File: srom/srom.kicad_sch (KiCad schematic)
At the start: 18 parts, among them J1 Conn_01x03_Female, Q1 PMBT2222A, U1 4075, U4 74LS245, U5 Pico-1 ROM

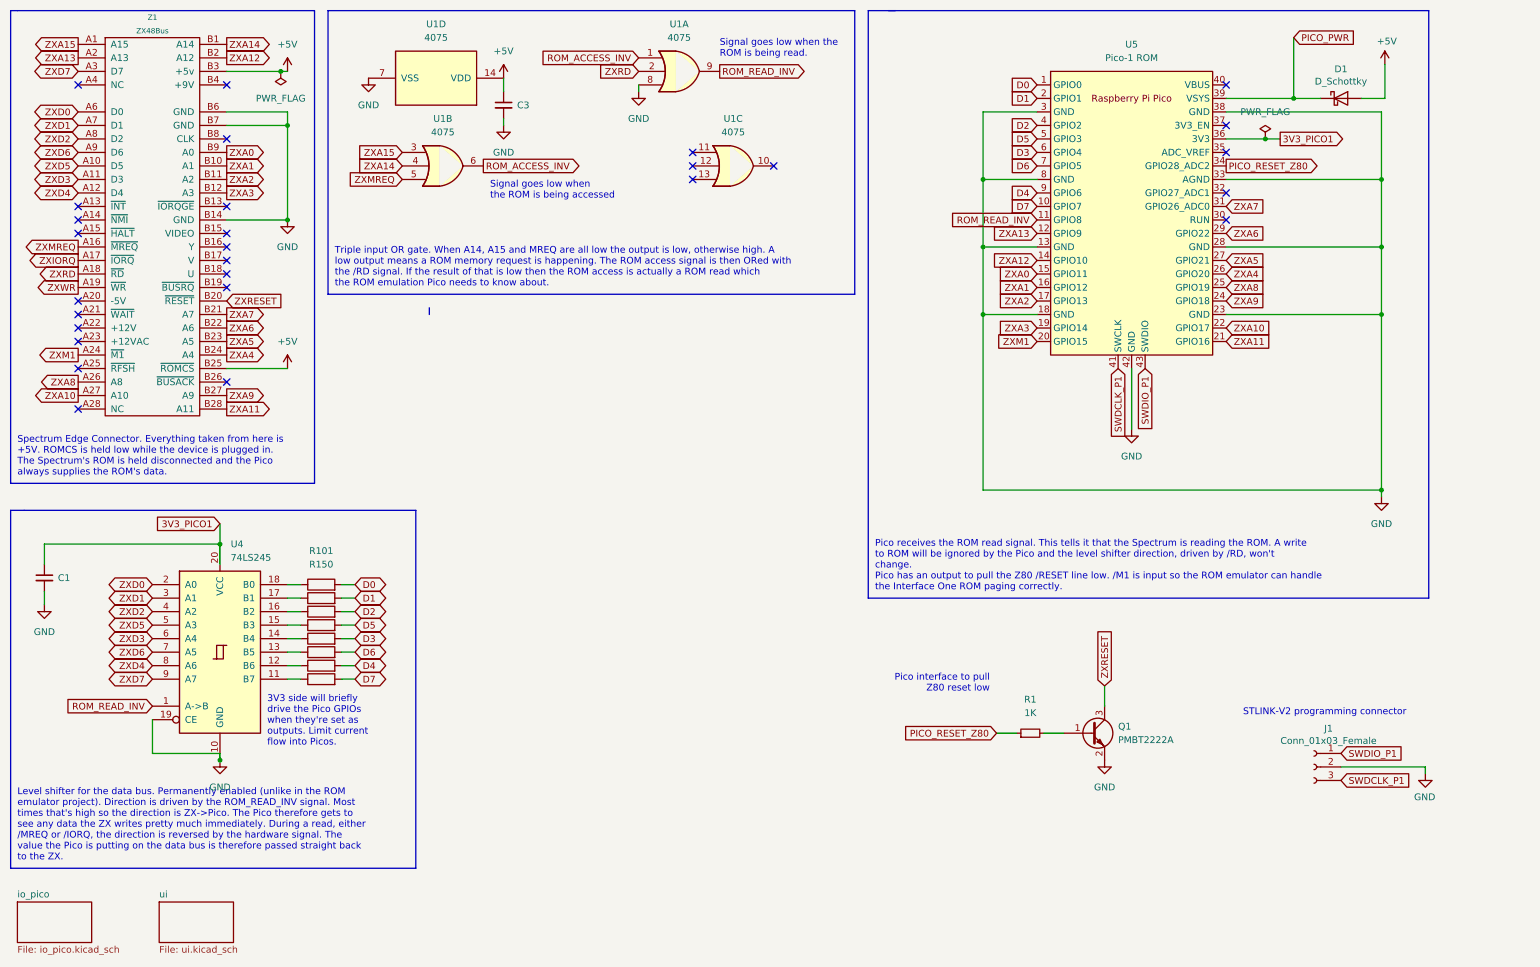
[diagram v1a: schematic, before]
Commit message: update schematic to match my modified prototype hardware
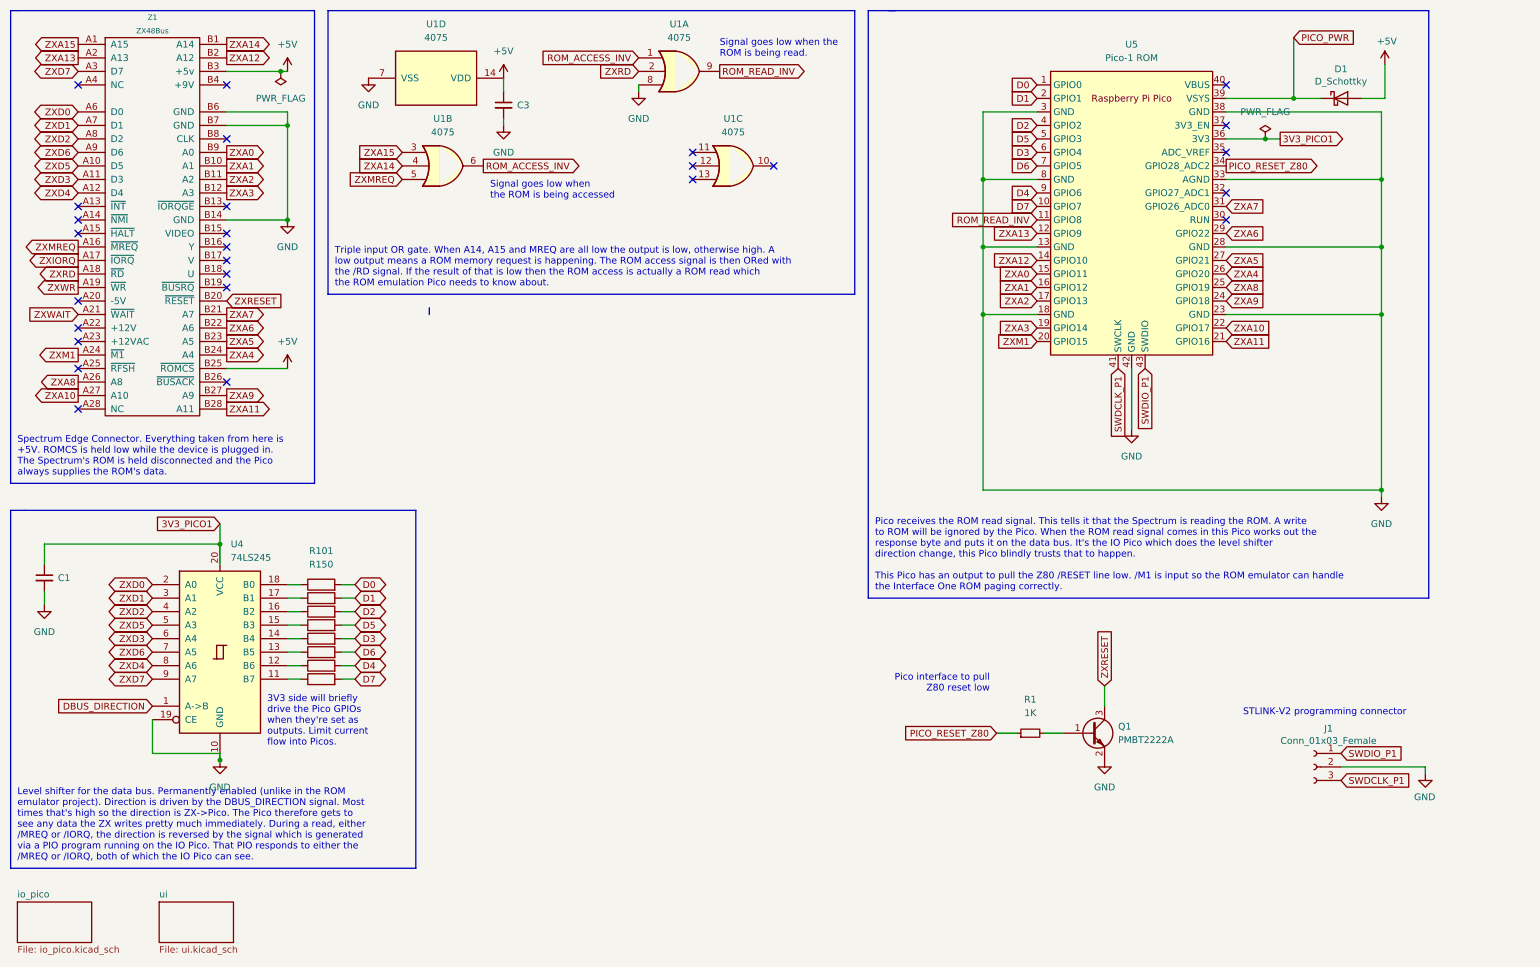
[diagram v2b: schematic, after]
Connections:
- net ROM_READ_INV: no longer U4.1 (A->B)
- net ZXWAIT: now reaches Z1.A21 (~{WAIT})
- new net DBUS_DIRECTION: U4.1 (A->B)
- no-connect marks 28 -> 27
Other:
- note added: "Level shifter for the data bus. Permanently enabled (unlike in the ROM emulator project). Direction is driven by the DBUS_DIRECTION signal. Most times that's high so the direction is ZX->Pico. The Pico therefore gets to see any data the ZX writes pretty much immediately. During a read, either /MREQ or /IORQ, the direction is reversed by the signal which is generated via a PIO program running on t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"
- note added: "Pico receives the ROM read signal. This tells it that the Spectrum is reading the ROM. A write to ROM will be ignored by the Pico. When the ROM read signal comes in this Pico works out the response byte and puts it on the data bus. It's the IO Pico which does the level shifter direction change, this Pico blindly trusts that to happen. This Pico has an output to pull the Z80 /RESET line low. /M1 i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"
- note removed: "Level shifter for the data bus. Permanently enabled (unlike in the ROM emulator project). Direction is driven by the ROM_READ_INV signal. Most times that's high so the direction is ZX->Pico. The Pico therefore gets to see any data the ZX writes pretty much immediately. During a read, either /MREQ or /IORQ, the direction is reversed by the hardware signal. The value the Pico is putting on the data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"
- note removed: "Pico receives the ROM read signal. This tells it that the Spectrum is reading the ROM. A write to ROM will be ignored by the Pico and the level shifter direction, driven by /RD, won't change. Pico has an output to pull the Z80 /RESET line low. /M1 is input so the ROM emulator can handle the Interface One ROM paging correctly."
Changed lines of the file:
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@@
   (no_connect (at 242.57 36.83))
   (no_connect (at 142.24 46.99))
-  (no_connect (at 26.67 72.39))
   (no_connect (at 26.67 69.85))
   (no_connect (at 54.61 52.07))
@@
     (stroke (width 0) (type default) (color 0 0 0 0))
   )
-  (text "Pico receives the ROM read signal. This tells it that the Spectrum is reading the ROM. A write\nto ROM will be ignored by the Pico and the level shifter direction, driven by /RD, won't\nchange.\nPico has an output to pull the Z80 /RESET line low. /M1 is input so the ROM emulator can handle\nthe Interface One ROM paging correctly."
+  (text "Pico receives the ROM read signal. This tells it that the Spectrum is reading the ROM. A write\nto ROM will be ignored by the Pico. When the ROM read signal comes in this Pico works out the\nresponse byte and puts it on the data bus. It's the IO Pico which does the level shifter\ndirection change, this Pico blindly trusts that to happen.\n\nThis Pico has an output to pull the Z80 /RESET line low. /M1 is input so the ROM emulator can handle\nthe Interface One ROM paging correctly."
     (at 176.53 124.46 0)
     (effects (font (size 1.27 1.27)) (justify left bottom))
   )
-  (text "Level shifter for the data bus. Permanently enabled (unlike in the ROM\nemulator project). Direction is driven by the ROM_READ_INV signal. Most\ntimes that's high so the direction is ZX->Pico. The Pico therefore gets to\nsee any data the ZX writes pretty much immediately. During a read, either\n/MREQ or /IORQ, the direction is reversed by the hardware signal. The\nvalue the Pico is putting on the data bus is therefore passed straight back\nto the ZX."
+  (text "Level shifter for the data bus. Permanently enabled (unlike in the ROM\nemulator project). Direction is driven by the DBUS_DIRECTION signal. Most\ntimes that's high so the direction is ZX->Pico. The Pico therefore gets to\nsee any data the ZX writes pretty much immediately. During a read, either\n/MREQ or /IORQ, the direction is reversed by the signal which is generated\nvia a PIO program running on the IO Pico. That PIO responds to either the\n/MREQ or /IORQ, both of which the IO Pico can see."
     (at 15.24 175.26 0)
     (effects (font (size 1.27 1.27)) (justify left bottom))
@@
     )
   )
-  (global_label "ROM_READ_INV" (shape input) (at 40.64 146.05 180) (fields_autoplaced)
-    (effects (font (size 1.27 1.27)) (justify right))
-    (property "Intersheet References" "${INTERSHEET_REFS}" (id 0) (at 24.4383 145.9706 0)
+  (global_label "DBUS_DIRECTION" (shape input) (at 40.64 146.05 180) (fields_autoplaced)
+    (effects (font (size 1.27 1.27)) (justify right))
+    (property "Intersheet References" "${INTERSHEET_REFS}" (id 0) (at 22.3821 145.9706 0)
       (effects (font (size 1.27 1.27)) (justify right) hide)
     )
@@
     (property "Intersheet References" "${INTERSHEET_REFS}" (id 0) (at 163.5217 26.5906 0)
       (effects (font (size 1.27 1.27)) (justify left) hide)
+    )
+  )
+  (global_label "ZXWAIT" (shape input) (at 26.67 72.39 180) (fields_autoplaced)
+    (effects (font (size 1.27 1.27)) (justify right))
+    (property "Intersheet References" "${INTERSHEET_REFS}" (id 0) (at 17.7255 72.3106 0)
+      (effects (font (size 1.27 1.27)) (justify right) hide)
     )
   )
@@
       (reference "#PWR0203") (unit 1) (value "GND") (footprint "")
     )
-    (path "/95a6eb69-d4c1-4a7e-a8e8-144430faf0e2/e68adfe0-aa89-4590-b5db-e19a876b810c"
-      (reference "#PWR0204") (unit 1) (value "GND") (footprint "")
-    )
-    (path "/95a6eb69-d4c1-4a7e-a8e8-144430faf0e2/74d2792e-dc2e-4c26-bfe0-64794fa1d06e"
-      (reference "#PWR0207") (unit 1) (value "GND") (footprint "")
-    )
     (path "/95a6eb69-d4c1-4a7e-a8e8-144430faf0e2/81c696b0-3ffd-4923-88b9-a1f31d8f461a"
       (reference "#PWR0208") (unit 1) (value "GND") (footprint "")
@@
       (reference "C3") (unit 1) (value "C_Small") (footprint "Capacitor_SMD:C_1206_3216Metric")
     )
-    (path "/95a6eb69-d4c1-4a7e-a8e8-144430faf0e2/56c885f4-71dc-4c6a-84ef-761a4fa1779f"
-      (reference "C201") (unit 1) (value "C_Small") (footprint "Capacitor_SMD:C_1206_3216Metric")
-    )
     (path "/986f0686-4dd2-4d11-a20b-857347ffd112"
       (reference "D1") (unit 1) (value "D_Schottky") (footprint "Diode_SMD:D_1206_3216Metric_Pad1.42x1.75mm_HandSolder")
@@
       (reference "U201") (unit 1) (value "Pico-2 IO") (footprint "pico-foot:RPi_Pico_SMD_TH")
     )
-    (path "/95a6eb69-d4c1-4a7e-a8e8-144430faf0e2/45b2489c-7676-4f1b-a4c2-b602d5fb3354"
-      (reference "U202") (unit 1) (value "74LS245") (footprint "Package_SO:SO-20_5.3x12.6mm_P1.27mm")
-    )
     (path "/acda4c69-0a65-473b-ab4f-e765252d7da2/c3e5d4fc-20f0-4b23-a2a5-ed2745d1c377"

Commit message: start v1.3 of board, level shifter required
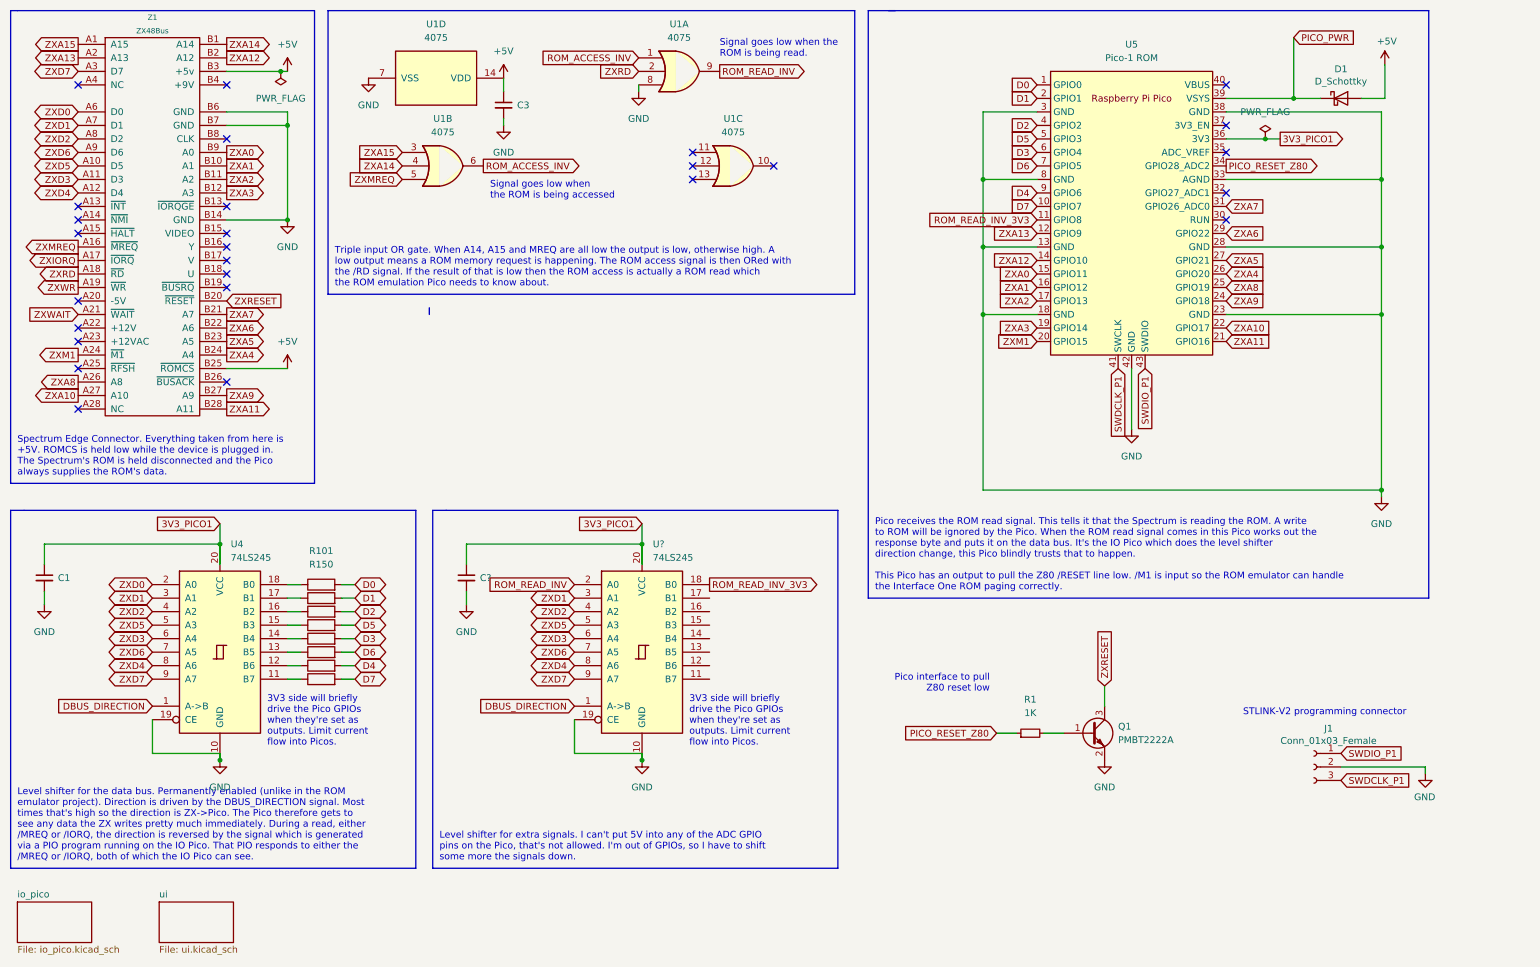
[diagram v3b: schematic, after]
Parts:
- added C?: C_Small, Capacitor_SMD:C_1206_3216Metric, symbol Device:C_Small
- added U?: 74LS245, Package_SO:SO-20_5.3x12.6mm_P1.27mm, symbol 74xx:74LS245
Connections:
- net 3V3_PICO1: now also C?.1, U?.20 (VCC)
- net DBUS_DIRECTION: now also U?.1 (A->B)
- net GND: now also C?.2, U?.10 (GND), U?.19 (CE)
- net ROM_READ_INV: now also U?.2 (A0); no longer U5.11 (GPIO8)
- net ZXD1: now also U?.3 (A1)
- net ZXD2: now also U?.4 (A2)
- net ZXD3: now also U?.6 (A4)
- net ZXD4: now also U?.8 (A6)
- net ZXD5: now also U?.5 (A3)
- net ZXD6: now also U?.7 (A5)
- net ZXD7: now also U?.9 (A7)
- new net ROM_READ_INV_3V3: U5.11 (GPIO8), U?.18 (B0)
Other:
- note added: "Level shifter for extra signals. I can't put 5V into any of the ADC GPIO pins on the Pico, that's not allowed. I'm out of GPIOs, so I have to shift some more the signals down."
